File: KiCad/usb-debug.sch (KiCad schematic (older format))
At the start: 77 parts, among them IC15 TLV70018DCKT, IC16 AP22652W6-7, IC7 HD3SS3220, J11 632723300011, Q1 PMV32UP, T6 BSS138APW, T7 BSS138APW

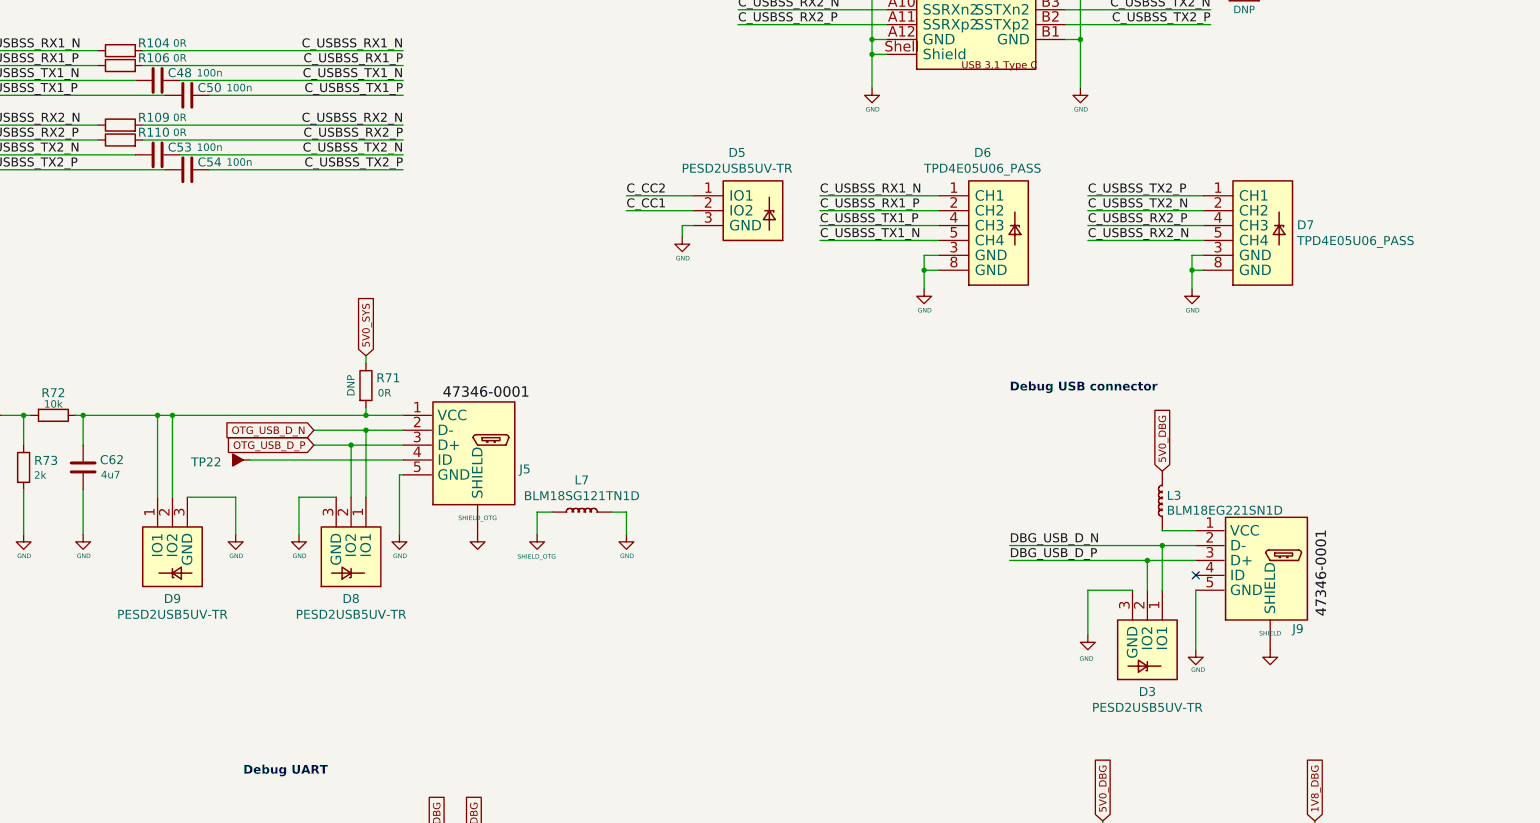
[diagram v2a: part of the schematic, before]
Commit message: Change PESD2USB5UV-TR and TPD4E05U06_PASS  to TPD4E05U06QDQARQ1
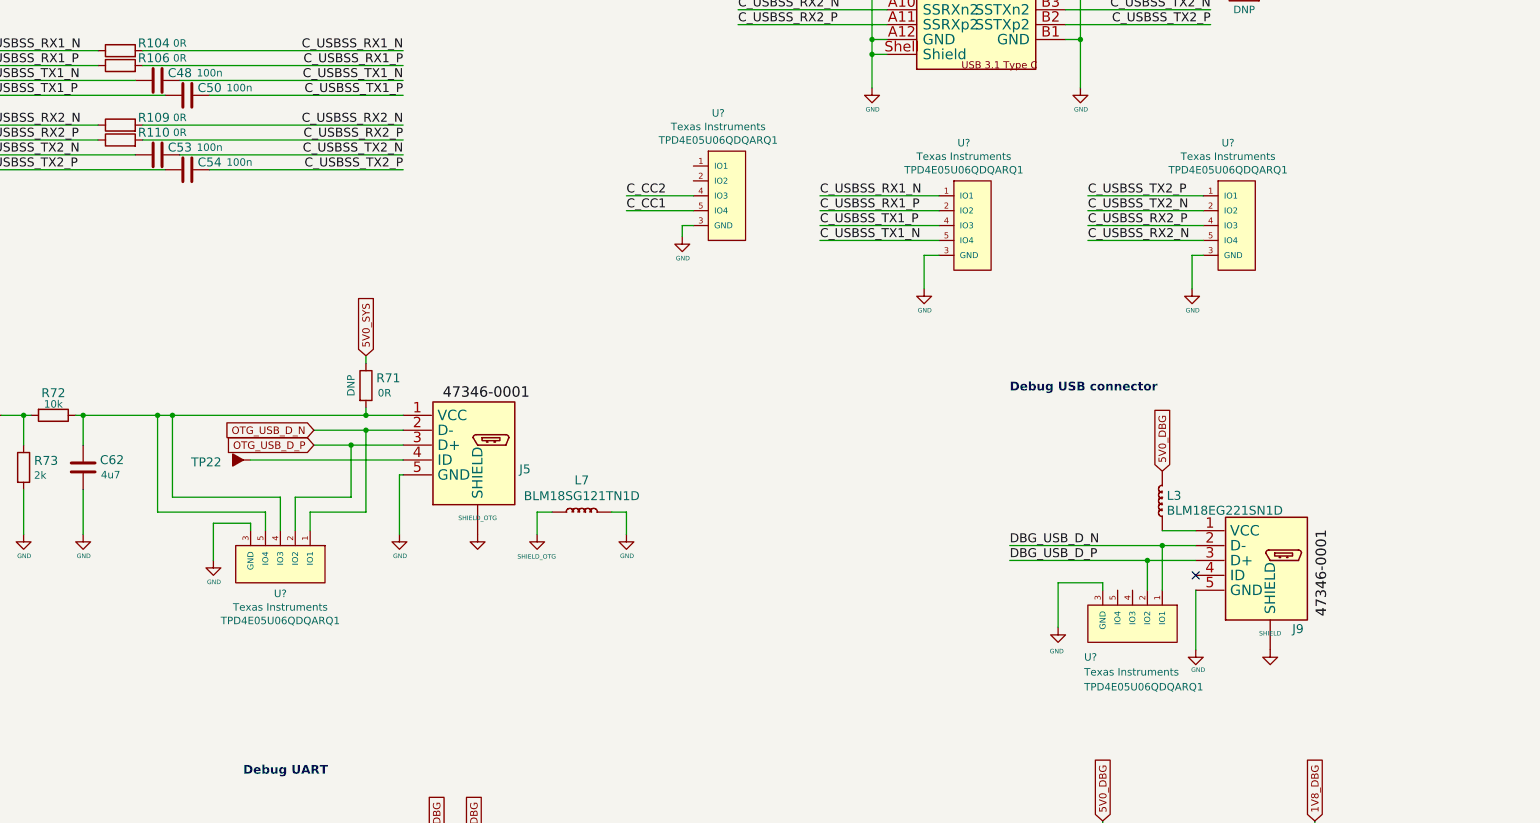
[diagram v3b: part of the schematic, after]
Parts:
- removed D3, D5, D8, D9: PESD2USB5UV-TR, jetson-nano-baseboard-footprints:SOT-23s, symbol jetson-nano-baseboard:PESD2USB5UV-TR
- removed D6, D7: TPD4E05U06_PASS, jetson-nano-baseboard-footprints:TPD4E05U06_PASS, symbol jetson-nano-baseboard:TPD4E05U06_PASS
- added U? (x5): TPD4E05U06QDQARQ1, jetson-nano-baseboard-footprints:TPD4E05U06QDQARQ1, symbol jetson-nano-baseboard:TPD4E05U06QDQARQ1
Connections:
- net C_CC1: now also U?.5 (IO4), U?.6 (IO4)
- net C_CC2: now also U?.4 (IO3), U?.7 (IO3)
- net C_USBSS_RX1_N: now also U?.1 (IO1), U?.10 (IO1)
- net C_USBSS_RX1_P: now also U?.2 (IO2), U?.9 (IO2)
- net C_USBSS_RX2_N: now also U?.5 (IO4), U?.6 (IO4)
- net C_USBSS_RX2_P: now also U?.4 (IO3), U?.7 (IO3)
- net C_USBSS_TX1_N: now also U?.5 (IO4), U?.6 (IO4)
- net C_USBSS_TX1_P: now also U?.4 (IO3), U?.7 (IO3)
- net C_USBSS_TX2_N: now also U?.2 (IO2), U?.9 (IO2)
- net C_USBSS_TX2_P: now also U?.1 (IO1), U?.10 (IO1)
- net DBG_USB_D_N: now also U?.1 (IO1), U?.10 (IO1)
- net DBG_USB_D_P: now also U?.2 (IO2), U?.9 (IO2)
- net GND: now also U?.3 (GND), U?.3 (GND), U?.3 (GND), U?.3 (GND), U?.3 (GND), U?.8 (GND), U?.8 (GND), U?.8 (GND), U?.8 (GND), U?.8 (GND)
- net OTG_USB_D_N: now also U?.1 (IO1), U?.10 (IO1)
- net OTG_USB_D_P: now also U?.2 (IO2), U?.9 (IO2)
- net at C62.2, J5.1 (VCC), R71.2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: now also U?.4 (IO3), U?.5 (IO4), U?.6 (IO4), U?.7 (IO3)
- new net: U?.1 (IO1), U?.10 (IO1)
- new net: U?.2 (IO2), U?.9 (IO2)
- new net: U?.4 (IO3), U?.7 (IO3)
- new net: U?.5 (IO4), U?.6 (IO4)
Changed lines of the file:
@@
 L jetson-nano-baseboard:GND #GND_087
 U 1 1 5E71036C
-P 12875 7425
-F 0 "#GND_087" H 12875 7425 20  0001 C CNN
-F 1 "GND" H 12866 7265 30  0000 C CNN
-F 2 "" H 12875 7425 70  0001 C CNN
-F 3 "" H 12875 7425 70  0001 C CNN
-	1    12875 7425
+P 12675 7375
+F 0 "#GND_087" H 12675 7375 20  0001 C CNN
+F 1 "GND" H 12666 7215 30  0000 C CNN
+F 2 "" H 12675 7375 70  0001 C CNN
+F 3 "" H 12675 7375 70  0001 C CNN
+	1    12675 7375
 	1    0    0    -1
 $EndComp
@@
 L jetson-nano-baseboard:GND #GND_0108
 U 1 1 5E710346
-P 7575 6750
-F 0 "#GND_0108" H 7575 6750 20  0001 C CNN
-F 1 "GND" H 7579 6605 30  0000 C CNN
-F 2 "" H 7575 6750 70  0001 C CNN
-F 3 "" H 7575 6750 70  0001 C CNN
-	1    7575 6750
+P 7000 6925
+F 0 "#GND_0108" H 7000 6925 20  0001 C CNN
+F 1 "GND" H 7004 6780 30  0000 C CNN
+F 2 "" H 7000 6925 70  0001 C CNN
+F 3 "" H 7000 6925 70  0001 C CNN
+	1    7000 6925
 	1    0    0    -1
 $EndComp
@@
 F 3 "" H 3050 9975 70  0001 C CNN
 	1    3050 9975
-	1    0    0    -1
-$EndComp
-$Comp
-L jetson-nano-baseboard:GND #GND_0113
-U 1 1 5E71033B
-P 7150 6750
-F 0 "#GND_0113" H 7150 6750 20  0001 C CNN
-F 1 "GND" H 7154 6605 30  0000 C CNN
-F 2 "" H 7150 6750 70  0001 C CNN
-F 3 "" H 7150 6750 70  0001 C CNN
-	1    7150 6750
 	1    0    0    -1
 $EndComp
@@
 Wire Wire Line
 	7925 6150 7675 6150
-Wire Wire Line
-	8025 6500 8025 6050
 Connection ~ 8025 6050
 Wire Wire Line
 	8025 6050 8275 6050
 Wire Wire Line
-	7825 6500 7575 6500
-Wire Wire Line
-	7575 6500 7575 6750
-Wire Wire Line
-	6825 6500 7150 6500
-Wire Wire Line
-	7150 6500 7150 6750
+	7250 6675 7000 6675
+Wire Wire Line
+	7000 6675 7000 6925
 Wire Wire Line
 	6725 6500 6725 5950
@@
 Wire Wire Line
 	6725 5950 6625 5950
-Wire Wire Line
-	6625 6500 6625 5950
 Connection ~ 6625 5950
 Wire Wire Line
@@
 	13600 6925 13275 6925
 Wire Wire Line
-	13175 7125 12875 7125
-Wire Wire Line
-	12875 7125 12875 7425
+	12675 7075 12675 7375
 Wire Wire Line
 	13275 7125 13275 6925
@@
 	11875 4875 11775 4875
 Wire Wire Line
-	11775 4875 11775 4975
-Wire Wire Line
-	11775 4975 11875 4975
-Connection ~ 11775 4975
-Wire Wire Line
-	11775 4975 11775 5100
-Wire Wire Line
 	12875 4475 13650 4475
 Wire Wire Line
@@
 Wire Wire Line
 	13650 4875 13575 4875
-Wire Wire Line
-	13575 4875 13575 4975
-Wire Wire Line
-	13650 4975 13575 4975
-Connection ~ 13575 4975
-Wire Wire Line
-	13575 4975 13575 5100
 Wire Wire Line
 	11525 2725 10425 2725
@@
 $EndComp
 $Comp
-L jetson-nano-baseboard:PESD2USB5UV-TR D9
-U 1 1 61BF6079
-P 6625 6700
-F 0 "D9" V 7108 6600 60  0000 C CNN
-F 1 "PESD2USB5UV-TR" V 7214 6600 60  0000 C CNN
-F 2 "jetson-nano-baseboard-footprints:SOT-23s" H 6675 6900 60  0001 C CNN
-F 3 "https://assets.nexperia.com/documents/data-sheet/PESD2USB5UV-T.pdf" H 6625 6700 60  0001 C CNN
-F 4 "PESD2USB5UV-TR " H 6325 7000 50  0001 C CNN "MPN"
-F 5 "Nexperia " H 6325 7100 50  0001 C CNN "Manufacturer"
-	1    6625 6700
-	0    -1   1    0
-$EndComp
-$Comp
-L jetson-nano-baseboard:PESD2USB5UV-TR D8
-U 1 1 61BFA215
-P 8025 6700
-F 0 "D8" V 8508 6600 60  0000 C CNN
-F 1 "PESD2USB5UV-TR" V 8614 6600 60  0000 C CNN
-F 2 "jetson-nano-baseboard-footprints:SOT-23s" H 8075 6900 60  0001 C CNN
-F 3 "https://assets.nexperia.com/documents/data-sheet/PESD2USB5UV-T.pdf" H 8025 6700 60  0001 C CNN
-F 4 "PESD2USB5UV-TR " H 7725 7000 50  0001 C CNN "MPN"
-F 5 "Nexperia " H 7725 7100 50  0001 C CNN "Manufacturer"
-	1    8025 6700
+L jetson-nano-baseboard:TPD4E05U06QDQARQ1 U?
+U 1 1 61FB5553
+P 7450 6775
+F 0 "U?" V 7823 6775 50  0000 C CNN
+F 1 "TPD4E05U06QDQARQ1" H 7500 6375 50  0001 L CNN
+F 2 "jetson-nano-baseboard-footprints:TPD4E05U06QDQARQ1" H 7500 7225 50  0001 L CNN
+F 3 "http://www.ti.com/general/docs/lit/getliterature.tsp?genericPartNumber=TPD4E001&fileType=pdf" H 7450 7175 50  0001 L CNN
+F 4 "Texas Instruments" V 7914 6775 50  0000 C CNN "Manufacturer"
+F 5 "TPD4E05U06QDQARQ1" V 8005 6775 50  0000 C CNN "MPN"
+	1    7450 6775
 	0    1    1    0
 $EndComp
 $Comp
-L jetson-nano-baseboard:PESD2USB5UV-TR D5
-U 1 1 61C529C6
-P 10425 4475
-F 0 "D5" H 10518 4764 60  0000 C CNN
-F 1 "PESD2USB5UV-TR" H 10518 4658 60  0000 C CNN
-F 2 "jetson-nano-baseboard-footprints:SOT-23s" H 10475 4675 60  0001 C CNN
-F 3 "https://assets.nexperia.com/documents/data-sheet/PESD2USB5UV-T.pdf" H 10425 4475 60  0001 C CNN
-F 4 "PESD2USB5UV-TR " H 10125 4775 50  0001 C CNN "MPN"
-F 5 "Nexperia " H 10125 4875 50  0001 C CNN "Manufacturer"
-	1    10425 4475
-	1    0    0    -1
-$EndComp
-$Comp
-L jetson-nano-baseboard:PESD2USB5UV-TR D3
-U 1 1 61C696B4
-P 13375 7325
-F 0 "D3" V 13858 7225 60  0000 C CNN
-F 1 "PESD2USB5UV-TR" V 13964 7225 60  0000 C CNN
-F 2 "jetson-nano-baseboard-footprints:SOT-23s" H 13425 7525 60  0001 C CNN
-F 3 "https://assets.nexperia.com/documents/data-sheet/PESD2USB5UV-T.pdf" H 13375 7325 60  0001 C CNN
-F 4 "PESD2USB5UV-TR " H 13075 7625 50  0001 C CNN "MPN"
-F 5 "Nexperia " H 13075 7725 50  0001 C CNN "Manufacturer"
-	1    13375 7325
+L jetson-nano-baseboard:TPD4E05U06QDQARQ1 U?
+U 1 1 61FBEC77
+P 10275 4475
+F 0 "U?" H 10392 5030 50  0000 C CNN
+F 1 "TPD4E05U06QDQARQ1" H 10325 4075 50  0001 L CNN
+F 2 "jetson-nano-baseboard-footprints:TPD4E05U06QDQARQ1" H 10325 4925 50  0001 L CNN
+F 3 "http://www.ti.com/general/docs/lit/getliterature.tsp?genericPartNumber=TPD4E001&fileType=pdf" H 10275 4875 50  0001 L CNN
+F 4 "Texas Instruments" H 10392 4939 50  0000 C CNN "Manufacturer"
+F 5 "TPD4E05U06QDQARQ1" H 10392 4848 50  0000 C CNN "MPN"
+	1    10275 4475
+	1    0    0    -1
+$EndComp
+$Comp
+L jetson-nano-baseboard:TPD4E05U06QDQARQ1 U?
+U 1 1 61FE29FF
+P 11925 4675
+F 0 "U?" H 12042 5230 50  0000 C CNN
+F 1 "TPD4E05U06QDQARQ1" H 11975 4275 50  0001 L CNN
+F 2 "jetson-nano-baseboard-footprints:TPD4E05U06QDQARQ1" H 11975 5125 50  0001 L CNN
+F 3 "http://www.ti.com/general/docs/lit/getliterature.tsp?genericPartNumber=TPD4E001&fileType=pdf" H 11925 5075 50  0001 L CNN
+F 4 "Texas Instruments" H 12042 5139 50  0000 C CNN "Manufacturer"
+F 5 "TPD4E05U06QDQARQ1" H 12042 5048 50  0000 C CNN "MPN"
+	1    11925 4675
+	1    0    0    -1
+$EndComp
+$Comp
+L jetson-nano-baseboard:TPD4E05U06QDQARQ1 U?
+U 1 1 61FF8D6D
+P 13700 4675
+F 0 "U?" H 13817 5230 50  0000 C CNN
+F 1 "TPD4E05U06QDQARQ1" H 13750 4275 50  0001 L CNN
+F 2 "jetson-nano-baseboard-footprints:TPD4E05U06QDQARQ1" H 13750 5125 50  0001 L CNN
+F 3 "http://www.ti.com/general/docs/lit/getliterature.tsp?genericPartNumber=TPD4E001&fileType=pdf" H 13700 5075 50  0001 L CNN
+F 4 "Texas Instruments" H 13817 5139 50  0000 C CNN "Manufacturer"
+F 5 "TPD4E05U06QDQARQ1" H 13817 5048 50  0000 C CNN "MPN"
+	1    13700 4675
+	1    0    0    -1
+$EndComp
+Wire Wire Line
+	13575 4875 13575 5100
+Wire Wire Line
+	11775 4875 11775 5100
+Wire Wire Line
+	12975 7075 12675 7075
+$Comp
+L jetson-nano-baseboard:TPD4E05U06QDQARQ1 U?
+U 1 1 62017093
+P 13175 7175
+F 0 "U?" V 13575 6850 50  0000 L CNN
+F 1 "TPD4E05U06QDQARQ1" H 13225 6775 50  0001 L CNN
+F 2 "jetson-nano-baseboard-footprints:TPD4E05U06QDQARQ1" H 13225 7625 50  0001 L CNN
+F 3 "http://www.ti.com/general/docs/lit/getliterature.tsp?genericPartNumber=TPD4E001&fileType=pdf" H 13175 7575 50  0001 L CNN
+F 4 "Texas Instruments" V 13675 6850 50  0000 L CNN "Manufacturer"
+F 5 "TPD4E05U06QDQARQ1" V 13775 6850 50  0000 L CNN "MPN"
+	1    13175 7175
 	0    1    1    0
 $EndComp
-$Comp
-L jetson-nano-baseboard:TPD4E05U06_PASS D6
-U 1 1 63492E55
-P 12075 4675
-F 0 "D6" H 12168 5164 60  0000 C CNN
-F 1 "TPD4E05U06_PASS" H 12168 5058 60  0000 C CNN
-F 2 "jetson-nano-baseboard-footprints:TPD4E05U06_PASS" H 12075 4675 60  0001 C CNN
-F 3 "" H 12075 4675 60  0001 C CNN
-F 4 "Texas Instruments" H 12075 4675 50  0001 C CNN "Manufacturer"
-F 5 "TPD4E05U06DQAR" H 12075 4675 50  0001 C CNN "MPN"
-	1    12075 4675
-	1    0    0    -1
-$EndComp
-$Comp
-L jetson-nano-baseboard:TPD4E05U06_PASS D7
-U 1 1 634A34A2
-P 13850 4675
-F 0 "D7" H 14280 4678 60  0000 L CNN
-F 1 "TPD4E05U06_PASS" H 14280 4572 60  0000 L CNN
-F 2 "jetson-nano-baseboard-footprints:TPD4E05U06_PASS" H 13850 4675 60  0001 C CNN
-F 3 "" H 13850 4675 60  0001 C CNN
-F 4 "Texas Instruments" H 13850 4675 50  0001 C CNN "Manufacturer"
-F 5 "TPD4E05U06DQAR" H 13850 4675 50  0001 C CNN "MPN"
-	1    13850 4675
-	1    0    0    -1
-$EndComp
+Wire Wire Line
+	12975 7075 12975 7125
+Wire Wire Line
+	7250 6675 7250 6725
+Wire Wire Line
+	6725 6500 7450 6500
+Wire Wire Line
+	7450 6500 7450 6725
+Wire Wire Line
+	6625 6600 7350 6600
+Wire Wire Line
+	7350 6600 7350 6725
+Wire Wire Line
+	6625 5950 6625 6600
+Wire Wire Line
+	7925 6500 7550 6500
+Wire Wire Line
+	7550 6500 7550 6725
+Wire Wire Line
+	8025 6600 7650 6600
+Wire Wire Line
+	7650 6600 7650 6725
+Wire Wire Line
+	8025 6050 8025 6600
 $EndSCHEMATC

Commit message: TLV70018DCKT -> TPS7A0518PDBVT
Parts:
- removed IC15: TLV70018DCKT, jetson-nano-baseboard-footprints:SC70-5, symbol jetson-nano-baseboard:TLV700
- removed L7: BLM18SG121TN1D, jetson-nano-baseboard-footprints:0603, symbol jetson-nano-baseboard:BLM18SG121TN1D
- added IC?: TPS7A0518PDBVT, antmicro-footprints:SOT-23-5, symbol antmicroPMICVoltageRegulatorsLinear:TPS7A0518PDBVT
- added U?: TPD4E05U06QDQARQ1, antmicro-footprints:TPD4E05U06QDQARQ1, symbol antmicroTVSDiodes:TPD4E05U06QDQARQ1
- U? (x5): footprint jetson-nano-baseboard-footprints:TPD4E05U06QDQARQ1 -> antmicro-footprints:TPD4E05U06QDQARQ1; symbol jetson-nano-baseboard:TPD4E05U06QDQARQ1 -> antmicroTVSDiodes:TPD4E05U06QDQARQ1
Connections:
- net 1V8_DBG: now also IC?.5 (VOUT)
- net 5V0_DBG: now also IC?.1 (VIN), IC?.3 (EN)
- net C_CC1: now also U?.2 (IO2), U?.9 (IO2); no longer U?.5 (IO4), U?.6 (IO4)
- net C_CC2: now also U?.1 (IO1), U?.10 (IO1); no longer U?.4 (IO3), U?.7 (IO3)
- net GND: now also IC?.2 (GND), U?.3 (GND), U?.8 (GND)
- net OTG_USB_D_N: now also U?.1 (IO1), U?.10 (IO1); no longer U?.1 (IO1), U?.10 (IO1)
- net OTG_USB_D_P: now also U?.2 (IO2), U?.9 (IO2); no longer U?.2 (IO2), U?.9 (IO2)
- net at C62.2, J5.1 (VCC), R71.2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: now also U?.1 (IO1), U?.10 (IO1), U?.2 (IO2), U?.9 (IO2); no longer U?.4 (IO3), U?.5 (IO4), U?.6 (IO4), U?.7 (IO3)
- new net: U?.4 (IO3), U?.7 (IO3) (x3)
- new net: U?.5 (IO4), U?.6 (IO4) (x3)
- no-connect marks 16 -> 18
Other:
- moved on the sheet: C67, U?
